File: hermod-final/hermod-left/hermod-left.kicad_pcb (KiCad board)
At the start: 2 copper layers, 183.9 x 155.8 mm, 196 parts, among them J1 USB_C_Receptacle_USB2.0, J2 Conn_01x05, J3 USB_C_Receptacle_USB2.0, Q1 AO3401A, Q2 MMUN2233LT1G, U1 STM32F072CBT6, U2 PRTR5V0U2X, U3 XC6206PxxxMR-Regulator_Linear, U4 CR2013-MI2120, U5 TXB0101

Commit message: Finished hermod designs
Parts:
- moved D39 0.49 mm to (184.7, 165.0)
- moved D38 0.49 mm to (169.1, 155.9)
- moved C39 0.27 mm to (186.5, 168.7)
- moved CH39 0.27 mm to (185.8, 162.0)
- moved LED39 0.27 mm to (189.9, 164.3)
- moved C38 0.26 mm to (171.2, 159.4)
- moved CH38 0.26 mm to (170.2, 153.0)
- moved LED38 0.26 mm to (174.3, 155.3)
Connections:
- U1 pad 12: /A2 -> col6
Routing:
- net col6: track 130.6 -> 165.6 mm, vias 3 -> 4
- net GND: track 240.8 -> 244.9 mm, vias 116 -> 120
- net Net-(LED38-DOUT): track 20.2 -> 20.9 mm
- net row0: track 190.3 -> 191.1 mm
- net row5: track 161.8 -> 161.2 mm

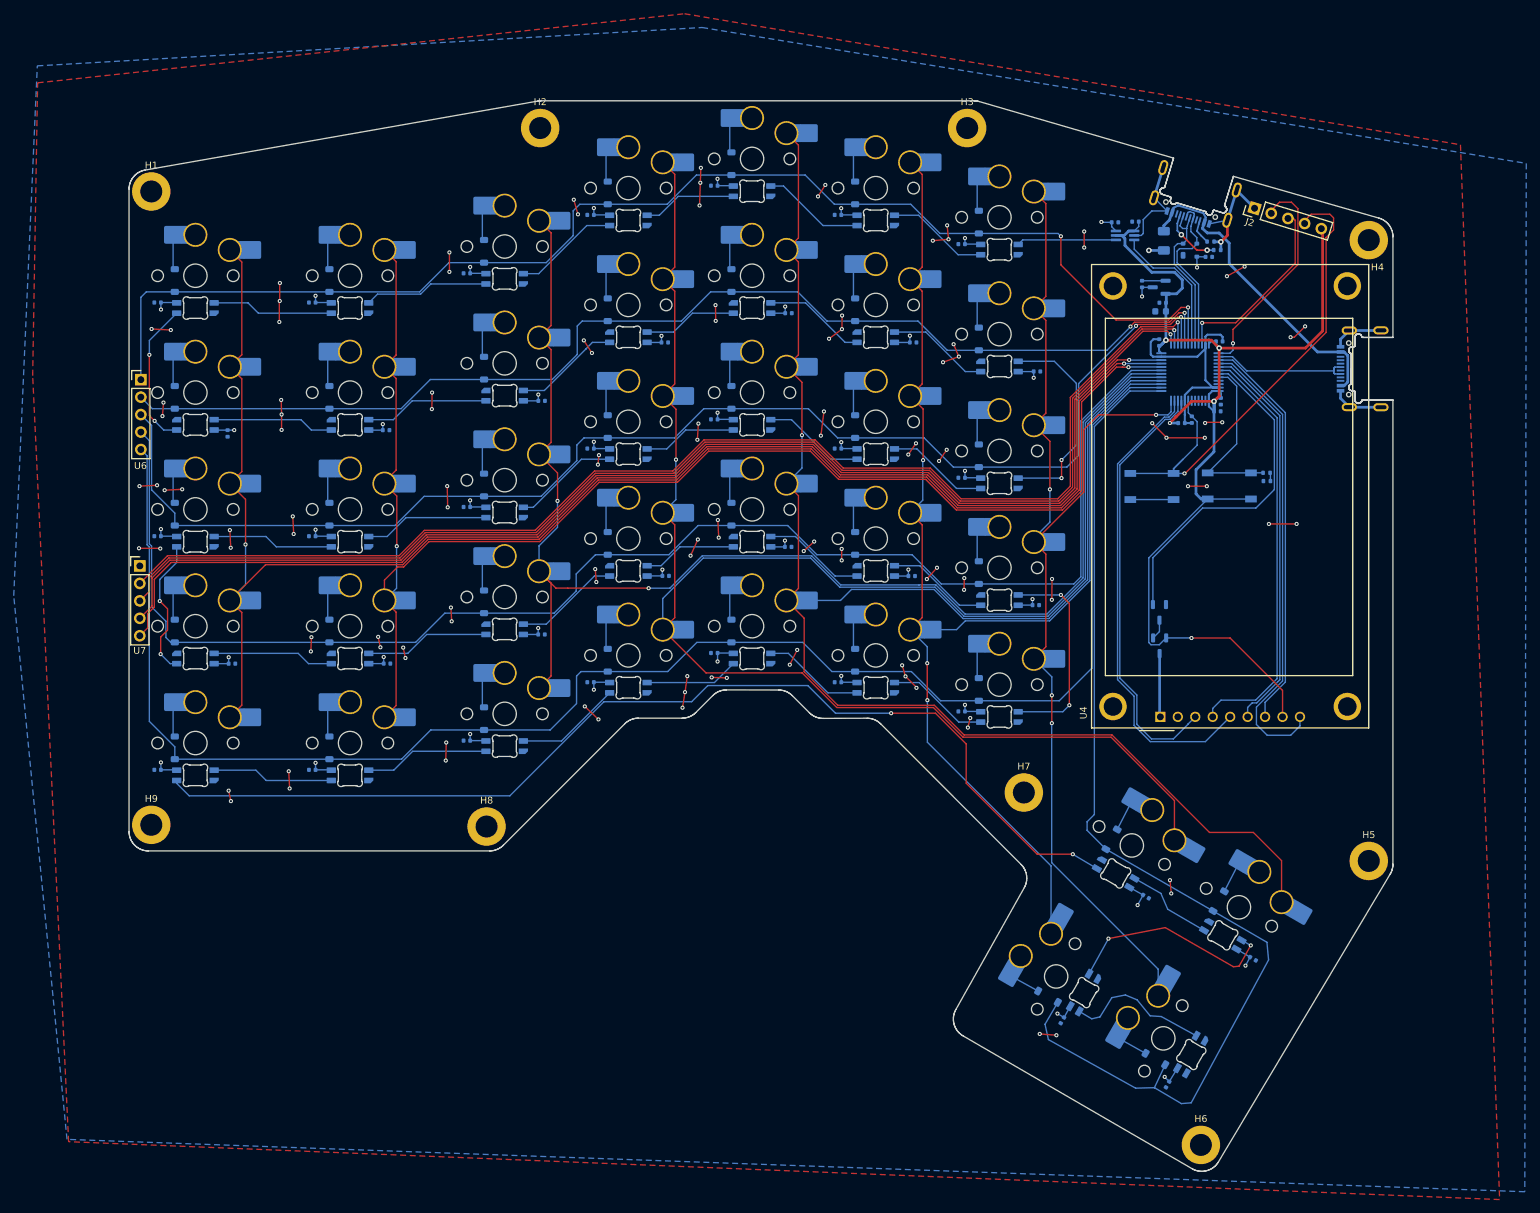
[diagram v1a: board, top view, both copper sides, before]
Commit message: Fixed random trace on numpad
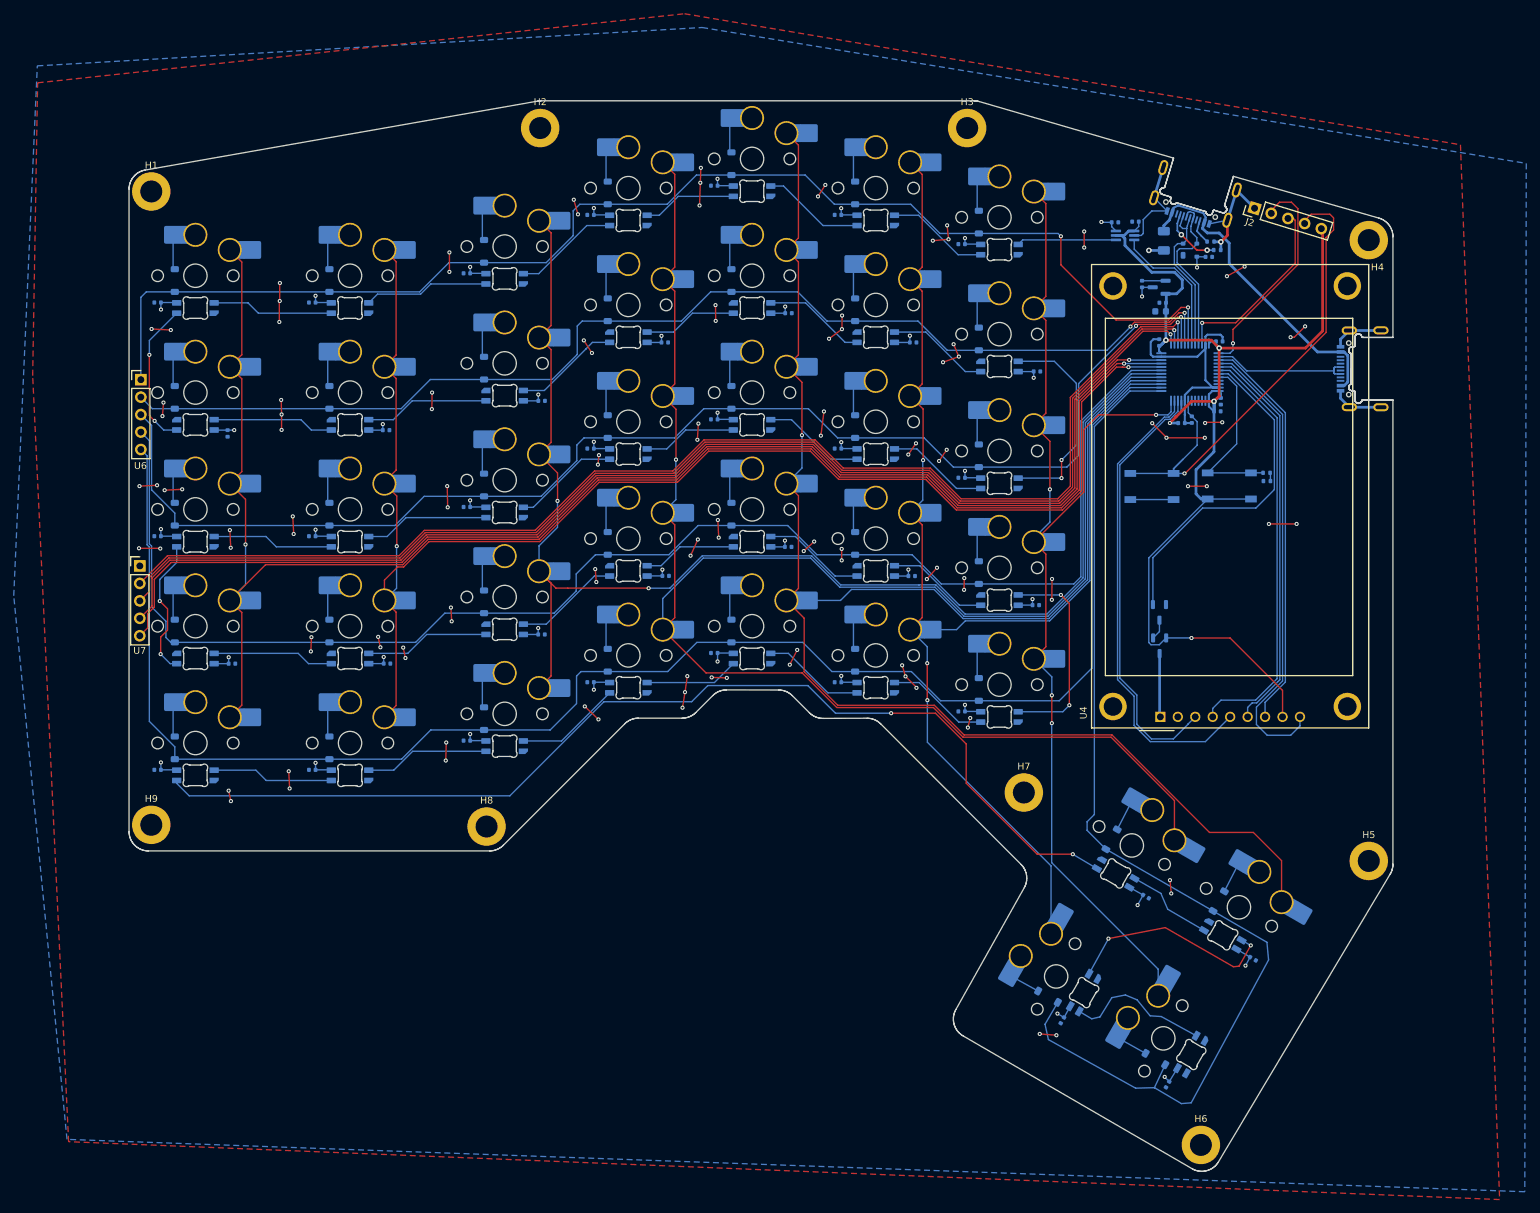
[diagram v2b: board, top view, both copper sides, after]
